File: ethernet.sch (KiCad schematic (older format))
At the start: 29 parts, among them U2 si3404, U3 ap2112, X1 SI-52003-F

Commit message: Move libs away from rescue. Re-constrained board layout since cutouts were not perpendicular (overconstrained)
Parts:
- D4, D5: symbol minipcie-eth-rescue:D_Bridge_+-AA -> minipcie-eth-rescue:D_Bridge_+-AA-minipcie-eth-rescue-minipcie-eth-rescue
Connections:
- net P0RN renamed PORN
- net P0RP renamed PORP
- net P0TN renamed POTN
- net P0TP renamed POTP
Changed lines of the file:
@@
 $EndDescr
 Text HLabel 1830 4540 2    60   Input ~ 0
-P0RN
+PORN
 Text HLabel 1830 4640 2    60   Input ~ 0
-P0RP
+PORP
 Text HLabel 1830 4940 2    60   Input ~ 0
-P0TP
+POTP
 Text HLabel 1830 4740 2    60   Input ~ 0
-P0TN
+POTN
 Text HLabel 10570 2000 2    60   Input ~ 0
 5V+_POE
@@
 $EndComp
 $Comp
-L minipcie-eth-rescue:D_Bridge_+-AA D5
+L minipcie-eth-rescue:D_Bridge_+-AA-minipcie-eth-rescue-minipcie-eth-rescue D5
 U 1 1 5BC20810
 P 2900 3790
+AR Path="/5BC20810" Ref="D5"  Part="1"
+AR Path="/5BAF0E8B/5BC20810" Ref="D5"  Part="1"
 F 0 "D5" H 3241 3836 50  0000 L CNN
 F 1 "VP/VN(1)" H 3241 3745 50  0000 L CNN
@@
 $EndComp
 $Comp
-L minipcie-eth-rescue:D_Bridge_+-AA D4
+L minipcie-eth-rescue:D_Bridge_+-AA-minipcie-eth-rescue-minipcie-eth-rescue D4
 U 1 1 5BC20875
 P 2890 4600
+AR Path="/5BC20875" Ref="D4"  Part="1"
+AR Path="/5BAF0E8B/5BC20875" Ref="D4"  Part="1"
 F 0 "D4" H 3231 4646 50  0000 L CNN
 F 1 "VP/VN(2)" H 3231 4555 50  0000 L CNN

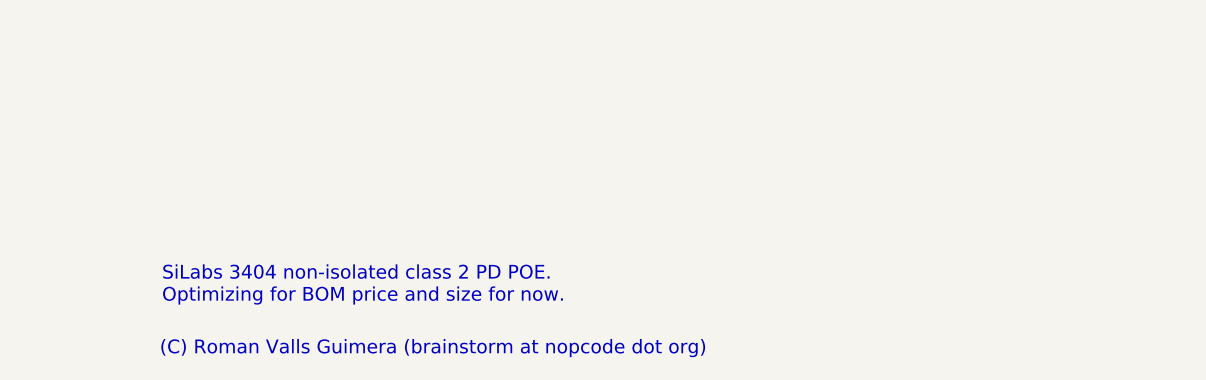
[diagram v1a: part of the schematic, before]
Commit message: Decided, I will switch to isolated si34061 design since the power budget and isolation are a bit too tight on the si3404... might change it all with the TPS23750 (https://www.ti.com/lit/ds/symlink/tps23770.pdf) in the future though
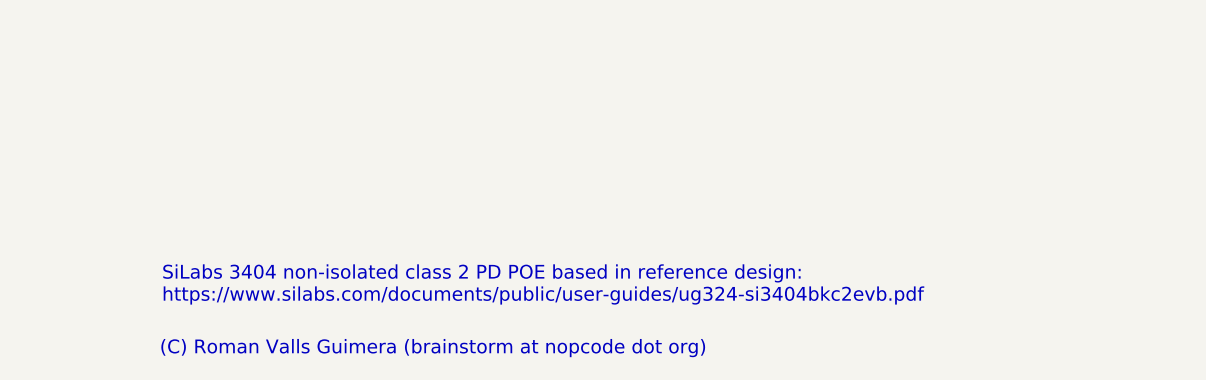
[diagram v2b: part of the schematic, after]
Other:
- note added: "SiLabs 3404 non-isolated class 2 PD POE based in reference design:\nhttps://www.silabs.com/documents/public/user-guides/ug324-si3404bkc2evb.pdf"
- note removed: "SiLabs 3404 non-isolated class 2 PD POE.\nOptimizing for BOM price and size for now."
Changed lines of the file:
@@
 $EndComp
 Text Notes 7000 6780 0    60   ~ 0
-SiLabs 3404 non-isolated class 2 PD POE.\nOptimizing for BOM price and size for now.
+SiLabs 3404 non-isolated class 2 PD POE based in reference design:\nhttps://www.silabs.com/documents/public/user-guides/ug324-si3404bkc2evb.pdf
 $Comp
 L device1:C_Small C2
